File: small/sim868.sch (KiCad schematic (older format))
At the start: 33 parts, among them IC2 SIM808, J1 78800-0001, J10 Conn_01x06_Female, J11 Conn_Coaxial, J12 Conn_Coaxial, Q1 2N7002, Q2 2N7002, Q3 2N7002, U16 SRV05-4

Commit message: BOM updated
Layout changed
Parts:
- C38, L3, R55: source (none) -> 0
- C43: MPN (none) -> CC0603KRX7R9BB104; Price (none) -> 0.0071; source (none) -> 0
- C45: MPN (none) -> CL10C470JB8NNNC; Price (none) -> 0.0078; source (none) -> 0
- C46, C51: MPN (none) -> TAJB107K006RNJ; Price (none) -> 0.2504; source (none) -> 0
- D11: Price (none) -> 0.0185; source (none) -> 0
- D12: MPN (none) -> 17-21SUYC/TR8; Price (none) -> 0.0142
- D13: MPN (none) -> FC-2012HRK-620D; Price (none) -> 0.0199; source (none) -> 0
- IC2: footprint SIM808 -> small:SIM808; MPN (none) -> SIM808; Manufacturer_Name SIMCOM -> (none); Manufacturer_Part_Number SIM808 -> (none)
- J1: footprint 788000001 -> small:788000001; MPN (none) -> 78800-0001; Manufacturer_Name Molex -> (none); Manufacturer_Part_Number 78800-0001 -> (none)
- Q1, Q2, Q3: LCSC (none) -> C8545; MPN (none) -> 2N7002; Price (none) -> 0.0219; source (none) -> 0
- R40, R42, R47, R48, R49: MPN (none) -> 0603WAF5101T5E; Price (none) -> 0.0021; source (none) -> 0
- R41, R46: MPN (none) -> 0603WAF1001T5E; source (none) -> 0
- R43, R44, R45: MPN (none) -> 0603WAF220JT5E; Price (none) -> 0.0022; source (none) -> 0
- R50, R51: MPN (none) -> 0603WAF2000T5E; Price (none) -> 0.0022; source (none) -> 0
- U16: MPN (none) -> SRV05-4-P-T7; source (none) -> 0
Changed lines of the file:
@@
 F 3 "https://datasheet.lcsc.com/szlcsc/Uniroyal-Elec-0603WAF5101T5E_C23186.pdf" H 8450 3325 50  0001 C CNN
 F 4 "C23186" V 8450 3325 50  0001 C CNN "LCSC"
+F 5 "0603WAF5101T5E" H 8450 3325 50  0001 C CNN "MPN"
+F 6 "0.0021" H 8450 3325 50  0001 C CNN "Price"
+F 7 "0" H 8450 3325 50  0001 C CNN "source"
 	1    8450 3325
 	-1   0    0    1
@@
 F 2 "Package_TO_SOT_SMD:SOT-23" H 9000 3100 50  0001 L CIN
 F 3 "https://www.onsemi.com/pub/Collateral/NDS7002A-D.PDF" H 8800 3175 50  0001 L CNN
+F 4 "C8545" H 8800 3175 50  0001 C CNN "LCSC"
+F 5 "2N7002" H 8800 3175 50  0001 C CNN "MPN"
+F 6 "0.0219" H 8800 3175 50  0001 C CNN "Price"
+F 7 "0" H 8800 3175 50  0001 C CNN "source"
 	1    8800 3175
 	1    0    0    -1
@@
 F 3 "https://datasheet.lcsc.com/szlcsc/Uniroyal-Elec-0603WAF5101T5E_C23186.pdf" H 6875 3350 50  0001 C CNN
 F 4 "C23186" V 6875 3350 50  0001 C CNN "LCSC"
+F 5 "0603WAF5101T5E" H 6875 3350 50  0001 C CNN "MPN"
+F 6 "0.0021" H 6875 3350 50  0001 C CNN "Price"
+F 7 "0" H 6875 3350 50  0001 C CNN "source"
 	1    6875 3350
 	-1   0    0    1
@@
 F 2 "Package_TO_SOT_SMD:SOT-23" H 7425 3125 50  0001 L CIN
 F 3 "https://www.onsemi.com/pub/Collateral/NDS7002A-D.PDF" H 7225 3200 50  0001 L CNN
+F 4 "C8545" H 7225 3200 50  0001 C CNN "LCSC"
+F 5 "2N7002" H 7225 3200 50  0001 C CNN "MPN"
+F 6 "0.0219" H 7225 3200 50  0001 C CNN "Price"
+F 7 "0" H 7225 3200 50  0001 C CNN "source"
 	1    7225 3200
 	1    0    0    -1
@@
 F 3 "https://datasheet.lcsc.com/szlcsc/Uniroyal-Elec-0603WAF5101T5E_C23186.pdf" H 4200 5150 50  0001 C CNN
 F 4 "C23186" V 4200 5150 50  0001 C CNN "LCSC"
+F 5 "0603WAF5101T5E" H 4200 5150 50  0001 C CNN "MPN"
+F 6 "0.0021" H 4200 5150 50  0001 C CNN "Price"
+F 7 "0" H 4200 5150 50  0001 C CNN "source"
 	1    4200 5150
 	-1   0    0    1
@@
 F 0 "IC2" H 2900 1825 50  0000 L CNN
 F 1 "SIM808" H 4069 1730 50  0000 L CNN
-F 2 "SIM808" H 3875 3175 50  0001 L CNN
+F 2 "small:SIM808" H 3875 3175 50  0001 L CNN
 F 3 "http://simcom.ee/documents/SIM808/SIM808_Hardware%20Design_V1.02.pdf" H 3875 3075 50  0001 L CNN
 F 4 "GSM GPRS CELLULAR MODULE" H 3875 2975 50  0001 L CNN "Description"
 F 5 "" H 3875 2875 50  0001 L CNN "Height"
-F 6 "SIMCOM" H 3875 2775 50  0001 L CNN "Manufacturer_Name"
-F 7 "SIM808" H 3875 2675 50  0001 L CNN "Manufacturer_Part_Number"
+F 6 "" H 3875 2775 50  0001 L CNN "Manufacturer_Name"
+F 7 "" H 3875 2675 50  0001 L CNN "Manufacturer_Part_Number"
 F 8 "" H 3875 2575 50  0001 L CNN "Mouser Part Number"
 F 9 "" H 3875 2475 50  0001 L CNN "Mouser Price/Stock"
 F 10 "" H 3875 2375 50  0001 L CNN "Arrow Part Number"
 F 11 "" H 3875 2275 50  0001 L CNN "Arrow Price/Stock"
+F 12 "SIM808" H 1825 2575 50  0001 C CNN "MPN"
 	1    1825 2575
 	1    0    0    -1
@@
 F 3 "~" H 3925 5875 50  0001 C CNN
 F 4 "C23345" V 3925 5875 50  0001 C CNN "LCSC"
+F 5 "0603WAF220JT5E" H 3925 5875 50  0001 C CNN "MPN"
+F 6 "0.0022" H 3925 5875 50  0001 C CNN "Price"
+F 7 "0" H 3925 5875 50  0001 C CNN "source"
 	1    3925 5875
 	0    1    1    0
@@
 F 3 "~" H 3925 5575 50  0001 C CNN
 F 4 "C23345" V 3925 5575 50  0001 C CNN "LCSC"
+F 5 "0603WAF220JT5E" H 3925 5575 50  0001 C CNN "MPN"
+F 6 "0.0022" H 3925 5575 50  0001 C CNN "Price"
+F 7 "0" H 3925 5575 50  0001 C CNN "source"
 	1    3925 5575
 	0    1    1    0
@@
 F 3 "https://datasheet.lcsc.com/szlcsc/Uniroyal-Elec-0603WAF5101T5E_C23186.pdf" H 350 3200 50  0001 C CNN
 F 4 "C23186" V 350 3200 50  0001 C CNN "LCSC"
+F 5 "0603WAF5101T5E" H 350 3200 50  0001 C CNN "MPN"
+F 6 "0.0021" H 350 3200 50  0001 C CNN "Price"
+F 7 "0" H 350 3200 50  0001 C CNN "source"
 	1    350  3200
 	-1   0    0    1
@@
 F 2 "Package_TO_SOT_SMD:SOT-23" H 900 2975 50  0001 L CIN
 F 3 "https://www.onsemi.com/pub/Collateral/NDS7002A-D.PDF" H 700 3050 50  0001 L CNN
+F 4 "C8545" H 700 3050 50  0001 C CNN "LCSC"
+F 5 "2N7002" H 700 3050 50  0001 C CNN "MPN"
+F 6 "0.0219" H 700 3050 50  0001 C CNN "Price"
+F 7 "0" H 700 3050 50  0001 C CNN "source"
 	1    700  3050
 	1    0    0    -1
@@
 F 3 "https://datasheet.lcsc.com/szlcsc/Uniroyal-Elec-0603WAF5101T5E_C23186.pdf" H 1050 4350 50  0001 C CNN
 F 4 "C23186" V 1050 4350 50  0001 C CNN "LCSC"
+F 5 "0603WAF5101T5E" H 1050 4350 50  0001 C CNN "MPN"
+F 6 "0.0021" H 1050 4350 50  0001 C CNN "Price"
+F 7 "0" H 1050 4350 50  0001 C CNN "source"
 	1    1050 4350
 	-1   0    0    1
@@
 F 4 "C8062" H 6750 975 50  0001 C CNN "LCSC"
 F 5 "ZMM5V6" H 6750 975 50  0001 C CNN "MPN"
+F 6 "0.0185" H 6750 975 50  0001 C CNN "Price"
+F 7 "0" H 6750 975 50  0001 C CNN "source"
 	1    6750 975
 	0    1    1    0
@@
 F 5 "0.0526" H 7225 950 50  0001 C CNN "Price"
 F 6 "CL21A226MAQNNNE" H 7225 950 50  0001 C CNN "MPN"
+F 7 "0" H 7225 950 50  0001 C CNN "source"
 	1    7225 950
 	1    0    0    -1
@@
 F 3 "~" H 7600 950 50  0001 C CNN
 F 4 "C14663" H 7600 950 50  0001 C CNN "LCSC"
+F 5 "CC0603KRX7R9BB104" H 7600 950 50  0001 C CNN "MPN"
+F 6 "0.0071" H 7600 950 50  0001 C CNN "Price"
+F 7 "0" H 7600 950 50  0001 C CNN "source"
 	1    7600 950
 	1    0    0    -1
@@
 F 1 "47p" H 8040 905 50  0000 L CNN
 F 2 "Capacitor_SMD:C_0603_1608Metric" H 7963 800 50  0001 C CNN
-F 3 "~" H 7925 950 50  0001 C CNN
+F 3 "https://datasheet.lcsc.com/szlcsc/Samsung-Electro-Mechanics-CL10C470JB8NNNC_C1671.pdf" H 7925 950 50  0001 C CNN
 F 4 " C1671" H 7925 950 50  0001 C CNN "LCSC"
+F 5 "CL10C470JB8NNNC" H 7925 950 50  0001 C CNN "MPN"
+F 6 "0.0078" H 7925 950 50  0001 C CNN "Price"
+F 7 "0" H 7925 950 50  0001 C CNN "source"
 	1    7925 950
 	1    0    0    -1
@@
 F 3 "~" H 8350 950 50  0001 C CNN
 F 4 " C16133" H 8350 950 50  0001 C CNN "LCSC"
+F 5 "TAJB107K006RNJ" H 8350 950 50  0001 C CNN "MPN"
+F 6 "0.2504" H 8350 950 50  0001 C CNN "Price"
+F 7 "0" H 8350 950 50  0001 C CNN "source"
 	1    8350 950
 	1    0    0    -1
@@
 F 0 "J1" H 7825 5165 50  0000 C CNN
 F 1 "78800-0001" H 7825 5074 50  0000 C CNN
-F 2 "788000001" H 8175 5000 50  0001 L CNN
+F 2 "small:788000001" H 8175 5000 50  0001 L CNN
 F 3 "https://www.molex.com/pdm_docs/sd/788000001_sd.pdf" H 8175 4900 50  0001 L CNN
 F 4 "Molex 78800 Series Vertical Hinged Micro SIM Card Connector with SMT Termination" H 8175 4800 50  0001 L CNN "Description"
 F 5 "1" H 8175 4700 50  0001 L CNN "Height"
-F 6 "Molex" H 8175 4600 50  0001 L CNN "Manufacturer_Name"
-F 7 "78800-0001" H 8175 4500 50  0001 L CNN "Manufacturer_Part_Number"
+F 6 "" H 8175 4600 50  0001 L CNN "Manufacturer_Name"
+F 7 "" H 8175 4500 50  0001 L CNN "Manufacturer_Part_Number"
 F 8 "538-78800-0001" H 8175 4400 50  0001 L CNN "Mouser Part Number"
 F 9 "https://www.mouser.co.uk/ProductDetail/Molex/78800-0001/?qs=aW78vNDzAorsg%2FJdp7zzAQ%3D%3D" H 8175 4300 50  0001 L CNN "Mouser Price/Stock"
 F 10 "" H 8175 4200 50  0001 L CNN "Arrow Part Number"
 F 11 "" H 8175 4100 50  0001 L CNN "Arrow Price/Stock"
+F 12 "78800-0001" H 7325 4900 50  0001 C CNN "MPN"
 	1    7325 4900
 	1    0    0    -1
@@
 F 3 "~" H 3925 5675 50  0001 C CNN
 F 4 "C23345" V 3925 5675 50  0001 C CNN "LCSC"
+F 5 "0603WAF220JT5E" H 3925 5675 50  0001 C CNN "MPN"
+F 6 "0.0022" H 3925 5675 50  0001 C CNN "Price"
+F 7 "0" H 3925 5675 50  0001 C CNN "source"
 	1    3925 5675
 	0    1    1    0
@@
 F 3 "~" H 8775 950 50  0001 C CNN
 F 4 " C16133" H 8775 950 50  0001 C CNN "LCSC"
+F 5 "TAJB107K006RNJ" H 8775 950 50  0001 C CNN "MPN"
+F 6 "0.2504" H 8775 950 50  0001 C CNN "Price"
+F 7 "0" H 8775 950 50  0001 C CNN "source"
 	1    8775 950
 	1    0    0    -1
@@
 F 3 "https://datasheet.lcsc.com/szlcsc/Hubei-KENTO-Elec-17-21SUYC-TR8_C2296.pdf" H 7325 2425 50  0001 C CNN
 F 4 "C2296" V 7325 2425 50  0001 C CNN "LCSC"
+F 5 "17-21SUYC/TR8" H 7325 2425 50  0001 C CNN "MPN"
+F 6 "0.0142" H 7325 2425 50  0001 C CNN "Price"
 	1    7325 2425
 	0    -1   -1   0
@@
 F 3 "https://datasheet.lcsc.com/szlcsc/Uniroyal-Elec-0603WAF2000T5E_C8218.pdf" H 7325 2775 50  0001 C CNN
 F 4 "C8218" H 7325 2775 50  0001 C CNN "LCSC"
+F 5 "0603WAF2000T5E" H 7325 2775 50  0001 C CNN "MPN"
+F 6 "0.0022" H 7325 2775 50  0001 C CNN "Price"
+F 7 "0" H 7325 2775 50  0001 C CNN "source"
 	1    7325 2775
 	1    0    0    -1
@@
 F 3 "https://datasheet.lcsc.com/szlcsc/Hubei-KENTO-Elec-17-21SUYC-TR8_C2296.pdf" H 8900 2475 50  0001 C CNN
 F 4 "C84256" V 8900 2475 50  0001 C CNN "LCSC"
+F 5 "FC-2012HRK-620D" H 8900 2475 50  0001 C CNN "MPN"
+F 6 "0.0199" H 8900 2475 50  0001 C CNN "Price"
+F 7 "0" H 8900 2475 50  0001 C CNN "source"
 	1    8900 2475
 	0    -1   -1   0
@@
 F 3 "https://datasheet.lcsc.com/szlcsc/Uniroyal-Elec-0603WAF2000T5E_C8218.pdf" H 8900 2825 50  0001 C CNN
 F 4 "C8218" H 8900 2825 50  0001 C CNN "LCSC"
+F 5 "0603WAF2000T5E" H 8900 2825 50  0001 C CNN "MPN"
+F 6 "0.0022" H 8900 2825 50  0001 C CNN "Price"
+F 7 "0" H 8900 2825 50  0001 C CNN "source"
 	1    8900 2825
 	1    0    0    -1
@@
 F 3 "http://www.onsemi.com/pub/Collateral/SRV05-4-D.PDF" H 6250 6700 50  0001 C CNN
 F 4 "C85364" H 6250 6700 50  0001 C CNN "LCSC"
+F 5 "SRV05-4-P-T7" H 6250 6700 50  0001 C CNN "MPN"
+F 6 "0" H 6250 6700 50  0001 C CNN "source"
 	1    6250 6700
 	1    0    0    -1
@@
 F 5 "SDCL1608C27NJTDF" V 4575 3925 50  0001 C CNN "MPN"
 F 6 "0.0119" V 4575 3925 50  0001 C CNN "Price"
+F 7 "0" H 4575 3925 50  0001 C CNN "source"
 	1    4575 3925
 	0    1    1    0
@@
 F 5 "0603WAF5100T5E" H 4575 3450 50  0001 C CNN "MPN"
 F 6 "0.0019" H 4575 3450 50  0001 C CNN "Price"
+F 7 "0" H 4575 3450 50  0001 C CNN "source"
 	1    4575 3450
 	1    0    0    -1
@@
 F 3 "~" H 700 3975 50  0001 C CNN
 F 4 " C21190" V 700 3975 50  0001 C CNN "LCSC"
+F 5 "0603WAF1001T5E" H 700 3975 50  0001 C CNN "MPN"
+F 6 "0" H 700 3975 50  0001 C CNN "source"
 	1    700  3975
 	0    1    1    0
@@
 F 3 "~" H 700 3875 50  0001 C CNN
 F 4 " C21190" V 700 3875 50  0001 C CNN "LCSC"
+F 5 "0603WAF1001T5E" H 700 3875 50  0001 C CNN "MPN"
+F 6 "0" H 700 3875 50  0001 C CNN "source"
 	1    700  3875
 	0    1    1    0

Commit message: minor updates
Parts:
- R41, R46: Price (none) -> 0.009
- U16: Price (none) -> 0.1675
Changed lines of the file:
@@
 F 5 "SRV05-4-P-T7" H 6250 6700 50  0001 C CNN "MPN"
 F 6 "0" H 6250 6700 50  0001 C CNN "source"
+F 7 "0.1675" H 6250 6700 50  0001 C CNN "Price"
 	1    6250 6700
 	1    0    0    -1
@@
 F 5 "0603WAF1001T5E" H 700 3975 50  0001 C CNN "MPN"
 F 6 "0" H 700 3975 50  0001 C CNN "source"
+F 7 "0.009" H 700 3975 50  0001 C CNN "Price"
 	1    700  3975
 	0    1    1    0
@@
 F 5 "0603WAF1001T5E" H 700 3875 50  0001 C CNN "MPN"
 F 6 "0" H 700 3875 50  0001 C CNN "source"
+F 7 "0.009" H 700 3875 50  0001 C CNN "Price"
 	1    700  3875
 	0    1    1    0

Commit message: ENC28j60 package changed to soic 28 17.9
TODO: route
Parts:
- IC2, J1, J10, JP1, JP2: LCSC (none) -> N/A
- J11, J12: LCSC NA -> N/A
- R41, R46: LCSC C21190 -> C21190
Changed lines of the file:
@@
 F 11 "" H 3875 2275 50  0001 L CNN "Arrow Price/Stock"
 F 12 "SIM808" H 1825 2575 50  0001 C CNN "MPN"
+F 13 "N/A" H 1825 2575 50  0001 C CNN "LCSC"
 	1    1825 2575
 	1    0    0    -1
@@
 F 2 "Connector_PinHeader_2.54mm:PinHeader_1x06_P2.54mm_Vertical" H 1175 1775 50  0001 C CNN
 F 3 "~" H 1175 1775 50  0001 C CNN
+F 4 "N/A" H 1175 1775 50  0001 C CNN "LCSC"
 	1    1175 1775
 	1    0    0    -1
@@
 F 2 "Jumper:SolderJumper-2_P1.3mm_Open_RoundedPad1.0x1.5mm" H 1425 3975 50  0001 C CNN
 F 3 "~" H 1425 3975 50  0001 C CNN
+F 4 "N/A" H 1425 3975 50  0001 C CNN "LCSC"
 	1    1425 3975
 	1    0    0    -1
@@
 F 2 "Jumper:SolderJumper-2_P1.3mm_Open_RoundedPad1.0x1.5mm" H 1425 3875 50  0001 C CNN
 F 3 "~" H 1425 3875 50  0001 C CNN
+F 4 "N/A" H 1425 3875 50  0001 C CNN "LCSC"
 	1    1425 3875
 	1    0    0    -1
@@
 F 11 "" H 8175 4100 50  0001 L CNN "Arrow Price/Stock"
 F 12 "78800-0001" H 7325 4900 50  0001 C CNN "MPN"
+F 13 "N/A" H 7325 4900 50  0001 C CNN "LCSC"
 	1    7325 4900
 	1    0    0    -1
@@
 F 3 "https://eu.mouser.com/datasheet/2/276/1/0733910070_RF_COAX_CONNECTORS-173128.pdf" H 10500 900 50  0001 C CNN
 F 4 "73391-0070" H 10500 900 50  0001 C CNN "MPN"
-F 5 "NA" H 10500 900 50  0001 C CNN "LCSC"
+F 5 "N/A" H 10500 900 50  0001 C CNN "LCSC"
 F 6 "" H 10500 900 50  0001 C CNN "source"
 F 7 "mouser" H 10500 900 50  0001 C CNN "Website"
@@
 F 3 "https://eu.mouser.com/datasheet/2/276/1/0733910070_RF_COAX_CONNECTORS-173128.pdf" H 10500 1525 50  0001 C CNN
 F 4 "73391-0070" H 10500 1525 50  0001 C CNN "MPN"
-F 5 "NA" H 10500 1525 50  0001 C CNN "LCSC"
+F 5 "N/A" H 10500 1525 50  0001 C CNN "LCSC"
 F 6 "" H 10500 1525 50  0001 C CNN "source"
 F 7 "mouser" H 10500 1525 50  0001 C CNN "Website"
@@
 F 2 "Resistor_SMD:R_0603_1608Metric" V 630 3975 50  0001 C CNN
 F 3 "~" H 700 3975 50  0001 C CNN
-F 4 " C21190" V 700 3975 50  0001 C CNN "LCSC"
+F 4 "C21190" V 700 3975 50  0001 C CNN "LCSC"
 F 5 "0603WAF1001T5E" H 700 3975 50  0001 C CNN "MPN"
 F 6 "0" H 700 3975 50  0001 C CNN "source"
@@
 F 2 "Resistor_SMD:R_0603_1608Metric" V 630 3875 50  0001 C CNN
 F 3 "~" H 700 3875 50  0001 C CNN
-F 4 " C21190" V 700 3875 50  0001 C CNN "LCSC"
+F 4 "C21190" V 700 3875 50  0001 C CNN "LCSC"
 F 5 "0603WAF1001T5E" H 700 3875 50  0001 C CNN "MPN"
 F 6 "0" H 700 3875 50  0001 C CNN "source"

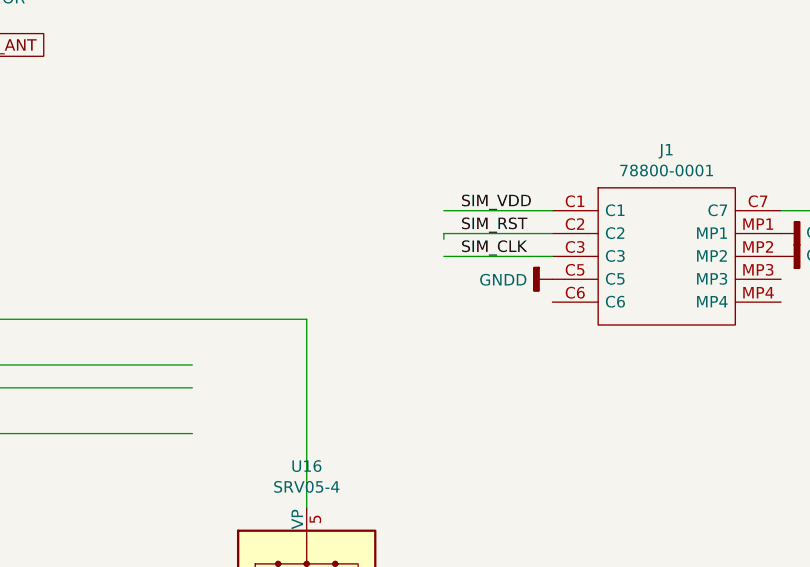
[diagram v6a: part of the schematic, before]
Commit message: capacitor added to sd card
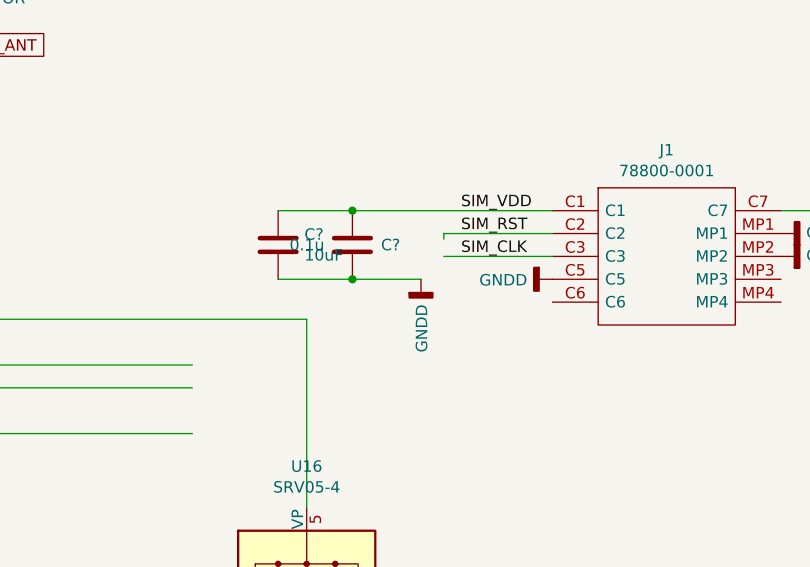
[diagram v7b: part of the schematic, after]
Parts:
- added C?: 0.1u, Capacitor_SMD:C_0603_1608Metric, symbol Device:C
- added C?: 10uF, Capacitor_SMD:C_1206_3216Metric, symbol Device:C
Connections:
- wire segments 83 -> 86
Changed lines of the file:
@@
 Text Label 4500 5375 0    50   ~ 0
 SIM_VDD
-Wire Wire Line
-	7325 4900 6850 4900
 Text Label 6925 4900 0    50   ~ 0
 SIM_VDD
@@
 Wire Wire Line
 	9525 900  10300 900
+$Comp
+L Device:C C?
+U 1 1 6035F703
+P 6450 5050
+AR Path="/6035F703" Ref="C?"  Part="1"
+AR Path="/6078415F/6035F703" Ref="C?"  Part="1"
+F 0 "C?" H 6575 5050 50  0000 L CNN
+F 1 "0.1u" H 6175 5050 50  0000 L CNN
+F 2 "Capacitor_SMD:C_0603_1608Metric" H 6488 4900 50  0001 C CNN
+F 3 "https://datasheet.lcsc.com/szlcsc/YAGEO-CC0603KRX7R9BB104_C14663.pdf" H 6450 5050 50  0001 C CNN
+F 4 "C14663" H 6450 5050 50  0001 C CNN "LCSC"
+F 5 "0.0071" H 6450 5050 50  0001 C CNN "Price"
+F 6 "CC0603KRX7R9BB104" H 6450 5050 50  0001 C CNN "MPN"
+F 7 "0" H 6450 5050 50  0001 C CNN "source"
+	1    6450 5050
+	1    0    0    -1
+$EndComp
+Connection ~ 6450 4900
+$Comp
+L Device:C C?
+U 1 1 6035F70F
+P 6125 5050
+AR Path="/6010B004/6035F70F" Ref="C?"  Part="1"
+AR Path="/6078415F/6035F70F" Ref="C?"  Part="1"
+F 0 "C?" H 6240 5096 50  0000 L CNN
+F 1 "10uF" H 6240 5005 50  0000 L CNN
+F 2 "Capacitor_SMD:C_1206_3216Metric" H 6163 4900 50  0001 C CNN
+F 3 "https://datasheet.lcsc.com/szlcsc/Samsung-Electro-Mechanics-CL31A106KBHNNNE_C13585.pdf" H 6125 5050 50  0001 C CNN
+F 4 "C13585" H 6125 5050 50  0001 C CNN "LCSC"
+F 5 "CL31A106KBHNNNE" H 6125 5050 50  0001 C CNN "MPN"
+F 6 "0" H 6125 5050 50  0001 C CNN "source"
+F 7 "0.0549" H 6125 5050 50  0001 C CNN "Price"
+	1    6125 5050
+	1    0    0    -1
+$EndComp
+Wire Wire Line
+	6125 5200 6450 5200
+Connection ~ 6450 5200
+Wire Wire Line
+	6450 5200 6750 5200
+Wire Wire Line
+	6125 4900 6450 4900
+Wire Wire Line
+	6450 4900 7325 4900
+$Comp
+L power:GNDD #PWR?
+U 1 1 6036A5CA
+P 6750 5200
+F 0 "#PWR?" H 6750 4950 50  0001 C CNN
+F 1 "GNDD" V 6754 5090 50  0000 R CNN
+F 2 "" H 6750 5200 50  0001 C CNN
+F 3 "" H 6750 5200 50  0001 C CNN
+	1    6750 5200
+	1    0    0    -1
+$EndComp
 $EndSCHEMATC

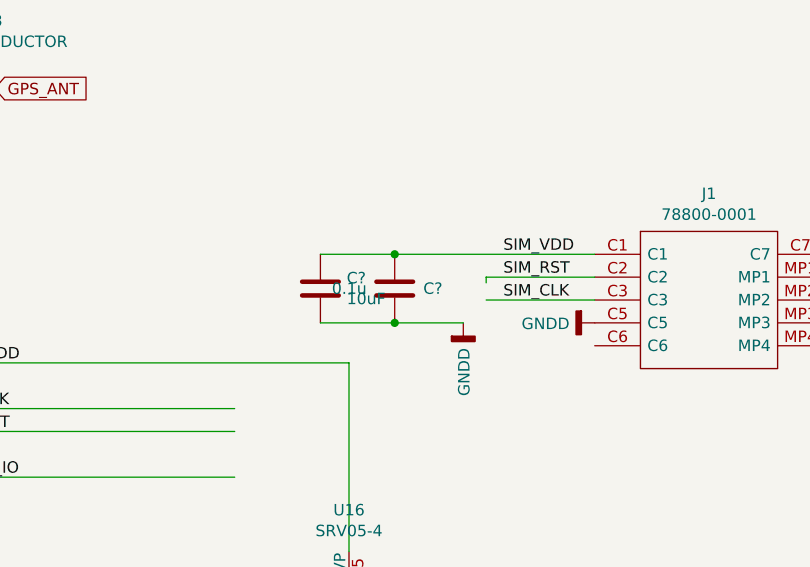
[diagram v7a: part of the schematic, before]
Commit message: Isolated DCDC added
power LED added
reverse voltage protection added
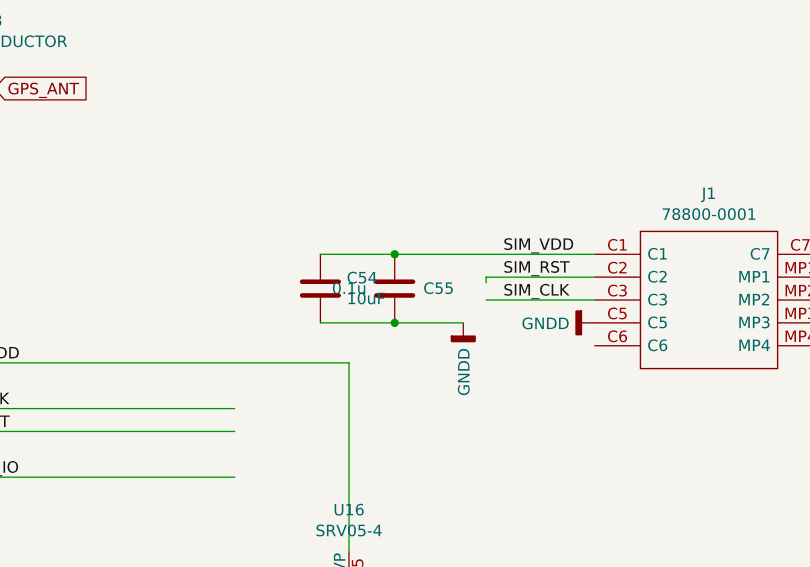
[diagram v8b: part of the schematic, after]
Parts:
- gave numbers to parts that had none: 2
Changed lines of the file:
@@
 AR Path="/6035F703" Ref="C?"  Part="1"
 AR Path="/6078415F/6035F703" Ref="C?"  Part="1"
-F 0 "C?" H 6575 5050 50  0000 L CNN
+AR Path="/602125D9/6035F703" Ref="C55"  Part="1"
+F 0 "C55" H 6575 5050 50  0000 L CNN
 F 1 "0.1u" H 6175 5050 50  0000 L CNN
 F 2 "Capacitor_SMD:C_0603_1608Metric" H 6488 4900 50  0001 C CNN
@@
 AR Path="/6010B004/6035F70F" Ref="C?"  Part="1"
 AR Path="/6078415F/6035F70F" Ref="C?"  Part="1"
-F 0 "C?" H 6240 5096 50  0000 L CNN
+AR Path="/602125D9/6035F70F" Ref="C54"  Part="1"
+F 0 "C54" H 6240 5096 50  0000 L CNN
 F 1 "10uF" H 6240 5005 50  0000 L CNN
 F 2 "Capacitor_SMD:C_1206_3216Metric" H 6163 4900 50  0001 C CNN
@@
 	6450 4900 7325 4900
 $Comp
-L power:GNDD #PWR?
+L power:GNDD #PWR0177
 U 1 1 6036A5CA
 P 6750 5200
-F 0 "#PWR?" H 6750 4950 50  0001 C CNN
+F 0 "#PWR0177" H 6750 4950 50  0001 C CNN
 F 1 "GNDD" V 6754 5090 50  0000 R CNN
 F 2 "" H 6750 5200 50  0001 C CNN
